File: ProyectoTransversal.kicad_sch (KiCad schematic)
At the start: 2 parts, among them J1 Conn_01x15, J2 Conn_01x15

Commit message: Add more components
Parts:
- removed J1, J2: Conn_01x15, symbol Connector_Generic:Conn_01x15
- added HS1: Heatsink, symbol Mechanical:Heatsink
- added J1, J2: Conn_01x19, symbol Connector_Generic:Conn_01x19
- added J3: Screw_Terminal_01x02, symbol Connector:Screw_Terminal_01x02
- added Q1: IRLZ44N, Package_TO_SOT_THT:TO-220-3_Vertical, symbol Transistor_FET:IRLZ44N
- added R1, R2, R3: R, symbol Device:R
- added U1: DS18B20, Package_TO_SOT_THT:TO-92_Inline, symbol Sensor_Temperature:DS18B20
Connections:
- net GND: now also J1.2 (Pin_2), J1.6 (Pin_6), R2.2, U1.1 (GND)
- net VIN: now also J1.1 (Pin_1)
- new net: R3.1, U1.3 (V_{DD})
- new net GATE: Q1.1 (G), R1.2
- new net PWM_OUT: R1.1, R2.1
- new net sensor_temp: R3.2, U1.2 (DQ)
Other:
- note added: "A diferencia de las resistencias o capacitores, el disipador muchas veces no se dibuja como un componente con "cables", sino como una anotación o un Footprint especial en la PCB."
- note added: "Ver tabla de pines"

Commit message: Continue
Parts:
- added D1: 1N4007, Diode_THT:D_DO-41_SOD81_P10.16mm_Horizontal, symbol Diode:1N4007
- added K1: Relay_SPDT, symbol Relay:Relay_SPDT
- added Q2: BC547, Package_TO_SOT_THT:TO-92_Inline, symbol Transistor_BJT:BC547
- added R4: R, symbol Device:R
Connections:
- net GND: now also J2.13 (Pin_13), J2.19 (Pin_19), Q1.3 (S), Q2.3 (E)
- net PWM_OUT: now also J2.18 (Pin_18)
- net sensor_temp: now also J2.11 (Pin_11)
- net 3V3: now reaches R3.1, U1.3 (V_{DD})
- net 3V3: now also J1.19 (Pin_19)
- net at Q1.2 (D): now also J3.1 (Pin_1)
- net SDA: now reaches J2.14 (Pin_14)
- net SCL: now reaches J2.17 (Pin_17)
- net CMD_Relay: now reaches J2.7 (Pin_7)
- new net: D1.2 (A), K1.A2, Q2.1 (C)
- new net: Q2.2 (B), R4.1
- new net 12V: K1.11
- new net 5V: D1.1 (K), K1.A1
- new net Alim_12V: K1.14
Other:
- note added: "Pull-Down"
- note added: "Pull-Up"
- moved on the sheet: J3

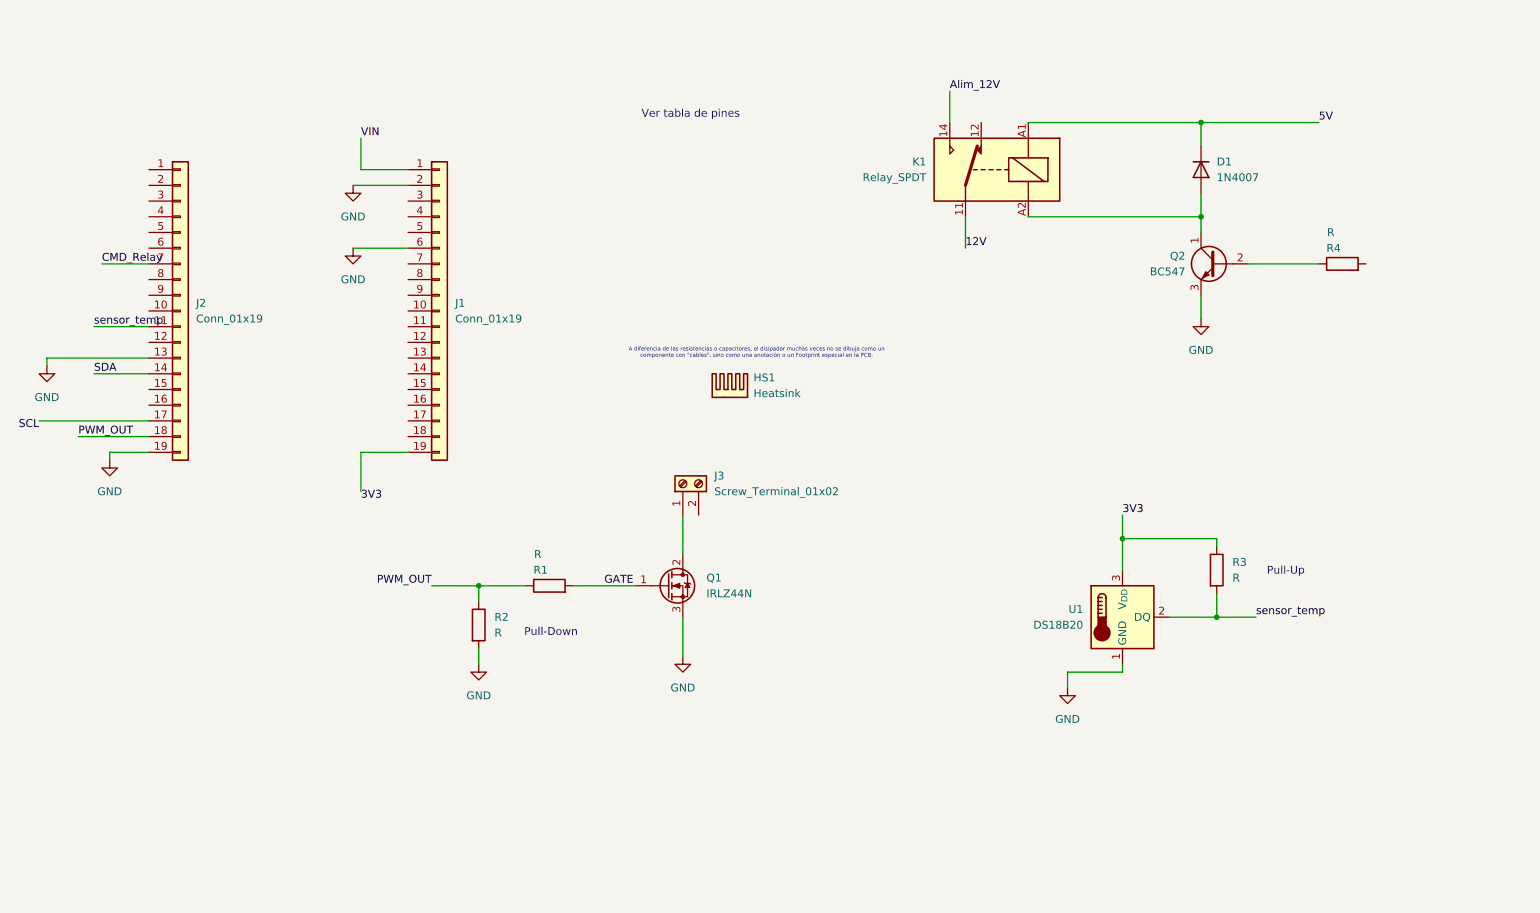
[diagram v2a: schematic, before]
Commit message: Add voltage regulator
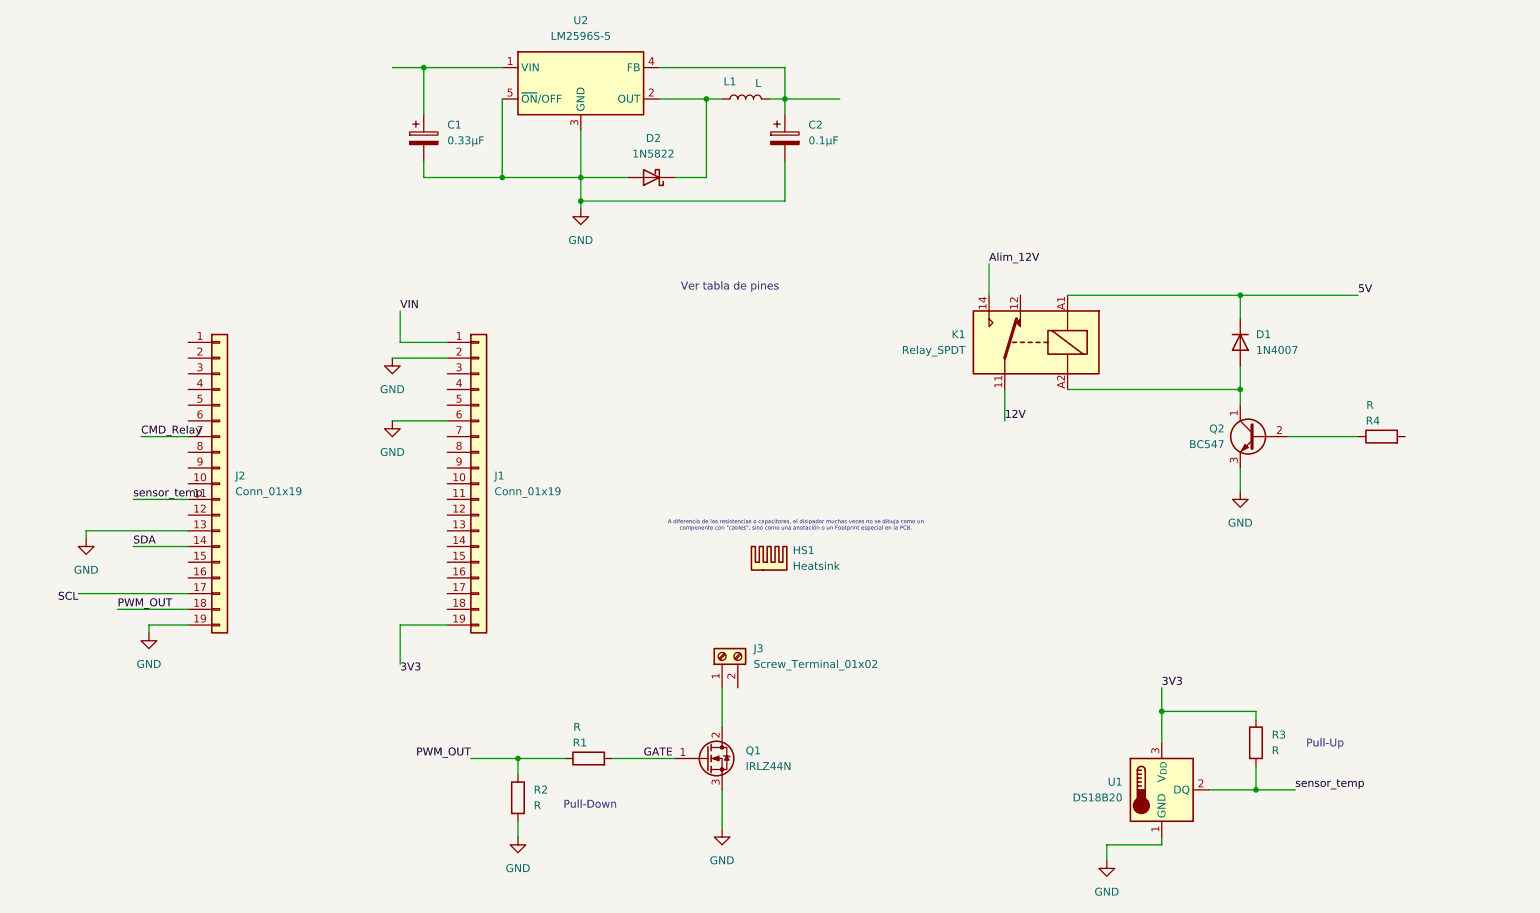
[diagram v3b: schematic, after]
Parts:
- added C1: 0.33µF, symbol Device:C_Polarized
- added C2: 0.1µF, symbol Device:C_Polarized
- added D2: 1N5822, Diode_THT:D_DO-201AD_P15.24mm_Horizontal, symbol Diode:1N5822
- added L1: L, symbol Device:L
- added U2: LM2596S-5, Package_TO_SOT_SMD:TO-263-5_TabPin3, symbol Regulator_Switching:LM2596S-5
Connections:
- net GND: now also C1.2, C2.2, D2.2 (A), U2.3 (GND), U2.5 (~{ON}/OFF)
- new net: C1.1, U2.1 (VIN)
- new net: D2.1 (K), L1.1, U2.2 (OUT)
- new net: C2.1, L1.2, U2.4 (FB)
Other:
- moved on the sheet: D1, HS1, J1, J2, J3, K1, Q1, Q2, R1, R2, R3, R4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

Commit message: Finish PCB connections and ERC
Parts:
- added J4: Screw_Terminal_01x02, symbol Connector:Screw_Terminal_01x02
- added J5: Conn_01x04, symbol Connector_Generic:Conn_01x04
- C1: value 0.33µF -> 220uF
- C2: value 0.1µF -> 100uF
- R1: value R -> 220
- R2: value R -> 10k
- R3: value R -> 4.7k
- R4: value R -> 1k
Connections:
- net 5V is gone; now on net V_reg: D1.1 (K), K1.A1
- net VIN is gone; now on net V_reg: J1.1 (Pin_1)
- net 12V: now also C1.1, U2.1 (VIN), J4.2 (Pin_2)
- net 3V3: now also J5.1 (Pin_1)
- net Alim_12V: now also J3.2 (Pin_2)
- net CMD_Relay: now also R4.2
- net GND: now also J4.1 (Pin_1), J5.4 (Pin_4)
- net SCL: now also J5.3 (Pin_3)
- net SDA: now also J5.2 (Pin_2)
- net V_reg: now reaches C2.1, L1.2, U2.4 (FB)
- no-connect marks 0 -> 28
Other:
- moved on the sheet: U1
